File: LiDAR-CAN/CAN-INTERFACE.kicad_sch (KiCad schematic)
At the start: 0 parts

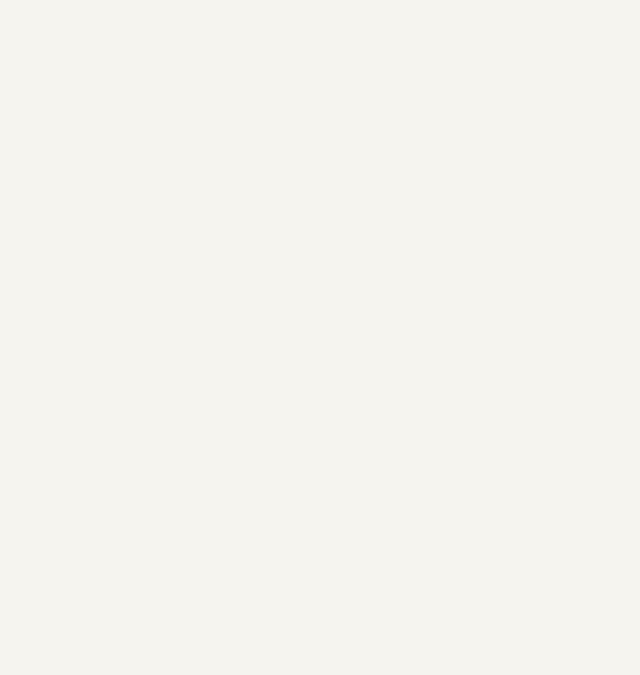
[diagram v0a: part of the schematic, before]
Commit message: Add main components in schematic sheets
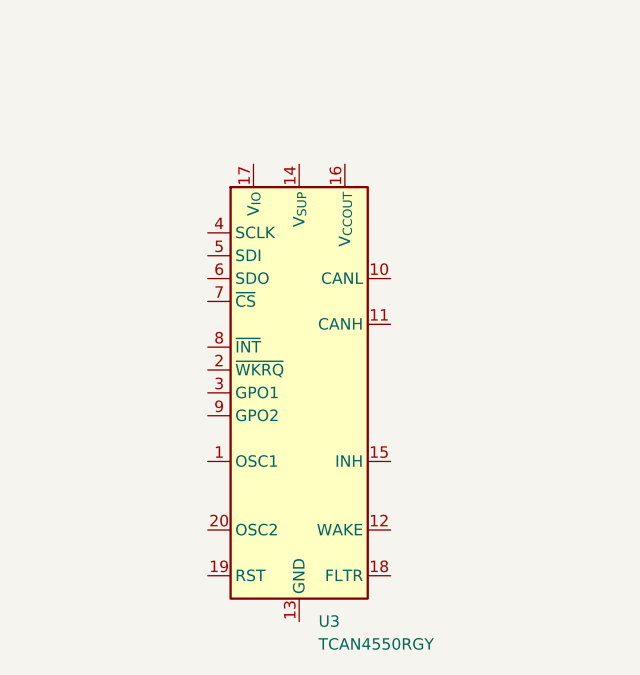
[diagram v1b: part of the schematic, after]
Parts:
- added U3: TCAN4550RGY, Package_DFN_QFN:Texas_RGY_R-PVQFN-N20_EP2.05x3.05mm, symbol Interface_CAN_LIN:TCAN4550RGY
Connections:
- new net: U3.13 (GND), U3.21 (GND)
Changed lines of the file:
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@@
+		)
+	)
+	(symbol
+		(lib_id "Interface_CAN_LIN:TCAN4550RGY")
+		(at 139.7 86.36 0)
+		(unit 1)
+		(exclude_from_sim no)
+		(in_bom yes)
+		(on_board yes)
+		(dnp no)
+		(fields_autoplaced yes)
+		(property "Reference" "U3"
+			(at 141.8433 111.76 0)
+			(effects
+				(font
+					(size 1.27 1.27)
+				)
+				(justify left)
+			)
+		)
+		(property "Value" "TCAN4550RGY"
+			(at 141.8433 114.3 0)
+			(effects
+				(font
+					(size 1.27 1.27)
+				)
+				(justify left)
+			)
+		)
+		(property "Footprint" "Package_DFN_QFN:Texas_RGY_R-PVQFN-N20_EP2.05x3.05mm"
+			(at 147.32 116.84 0)
+			(effects
+				(font
+					(size 1.27 1.27)
+					(italic yes)
+				)
+				(justify left)
+				(hide yes)
+			)
+		)
+		(property "Datasheet" "https://www.ti.com/lit/ds/symlink/tcan4550.pdf"
+			(at 147.32 114.3 0)
+			(effects
+				(font
+					(size 1.27 1.27)
+				)
+				(justify left)
+				(hide yes)
+			)
+		)
+		(property "Description" "CAN-FD controller with integrated transceiver, 5Mbps, 3.3V to 5V supply, SPI interface, VQFN-20"
+			(at 147.32 119.38 0)
+			(effects
+				(font
+					(size 1.27 1.27)
+				)
+				(justify left)
+				(hide yes)
+			)
+		)
+		(pin "5"
+		)
+		(pin "19"
+		)
+		(pin "16"
+		)
+		(pin "20"
+		)
+		(pin "4"
+		)
+		(pin "12"
+		)
+		(pin "8"
+		)
+		(pin "13"
+		)
+		(pin "6"
+		)
+		(pin "14"
+		)
+		(pin "3"
+		)
+		(pin "1"
+		)
+		(pin "2"
+		)
+		(pin "18"
+		)
+		(pin "9"
+		)
+		(pin "21"
+		)
+		(pin "10"
+		)
+		(pin "11"
+		)
+		(pin "15"
+		)
+		(pin "7"
+		)
+		(pin "17"
+		)
+		(instances
+			(project ""
+				(path "/56db6f21-0e4a-4321-bd8a-db37f1842dd9/acdb1e38-683e-41e3-b904-0eede9d7599d"
+					(reference "U3")
+					(unit 1)
+				)
+			)
 		)
 	)

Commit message: Add LiDAR Interface complete circuit
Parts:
- U3: Manufacturer (none) -> Texas Instruments
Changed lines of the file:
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@@
+			)
+		)
+		(property "Manufacturer" "Texas Instruments"
+			(at 139.7 86.36 0)
+			(effects
+				(font
+					(size 1.27 1.27)
+				)
+				(hide yes)
 			)
 		)

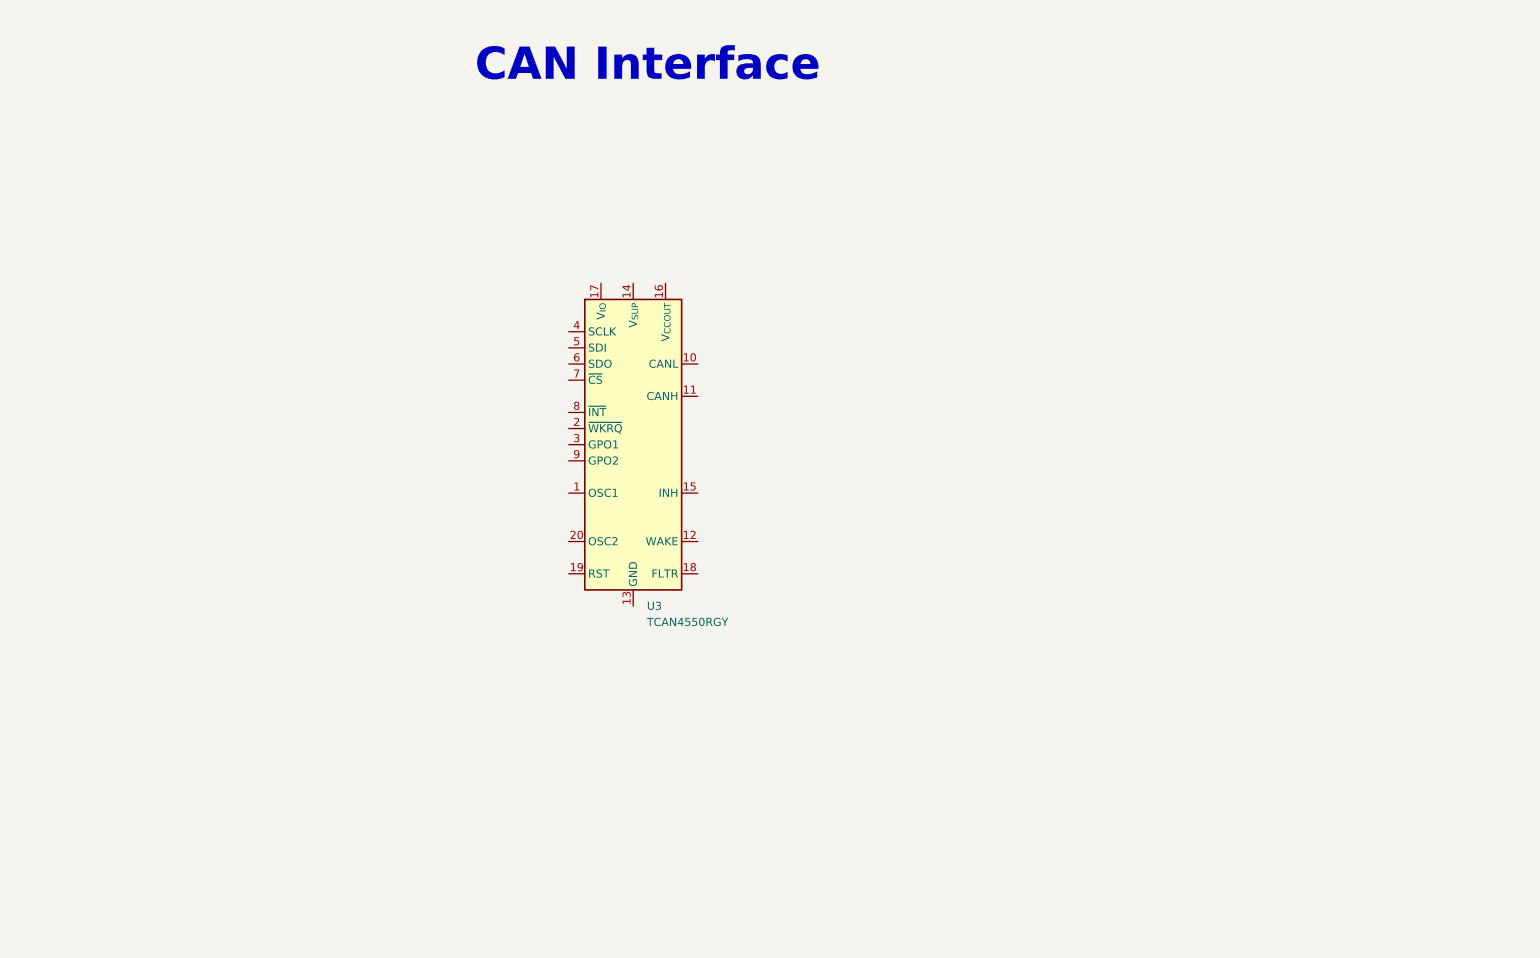
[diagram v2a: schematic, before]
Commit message: Add complete CAN Interface circuit
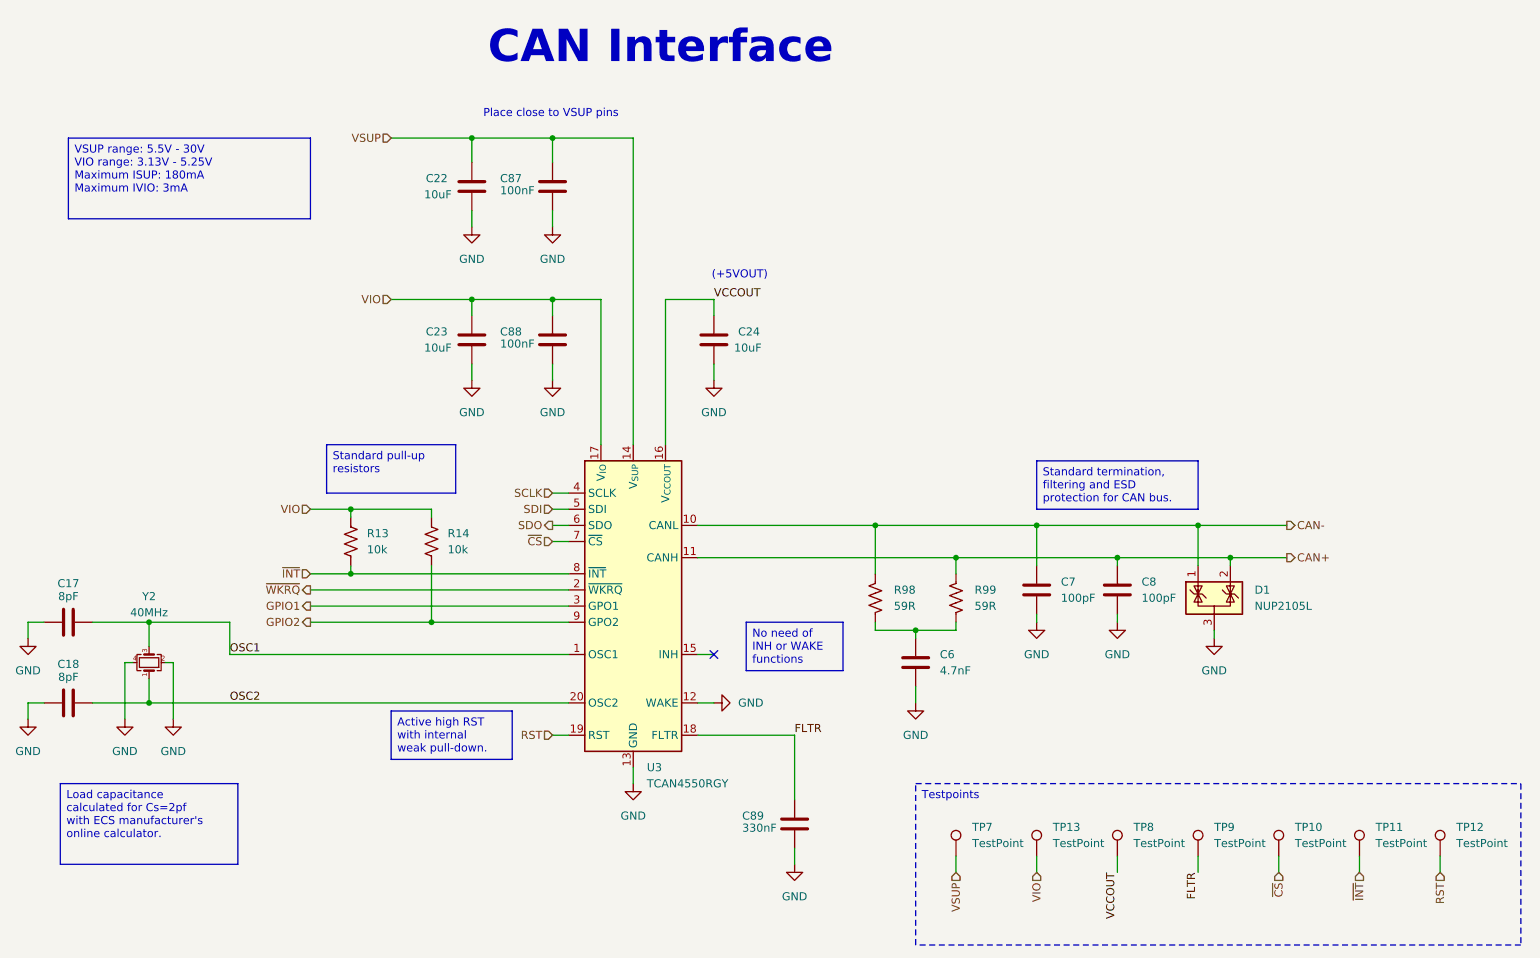
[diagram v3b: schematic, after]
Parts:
- added C17, C18: 8pF, Capacitor_SMD:C_0603_1608Metric, symbol Symbols:CAP CER 22PF 50V X7R 0603
- added C22, C23, C24: 10uF, Capacitor_SMD:C_0603_1608Metric, symbol Symbols:CAP CER 10UF 25V X5R 0603
- added C6: 4.7nF, Capacitor_SMD:C_0603_1608Metric, symbol Device:C
- added C7, C8: 100pF, Capacitor_SMD:C_0603_1608Metric, symbol Device:C
- added C87, C88: 100nF, Capacitor_SMD:C_0603_1608Metric, symbol Symbols:CAP CER 0.1UF 50V X7R 0603
- added C89: 330nF, Capacitor_SMD:C_0603_1608Metric, symbol Symbols:CAP CER 0.1UF 50V X7R 0603
- added D1: NUP2105L, Package_TO_SOT_SMD:SOT-23, symbol Power_Protection:NUP2105L
- added R13, R14: 10k, Resistor_SMD:R_0603_1608Metric, symbol Device:R_US
- added R98, R99: 59R, Resistor_SMD:R_0603_1608Metric, symbol Symbols:RES 1.2K OHM 5% 1/10W 0603
- added TP10, TP11, TP12, TP13, TP7, TP8, TP9: TestPoint, TestPoint:TestPoint_Pad_D1.5mm, symbol Connector:TestPoint
- added Y2: 40MHz, Crystal:Crystal_SMD_2016-4Pin_2.0x1.6mm, symbol Device:Crystal_GND24_Small
- U3: MPN (none) -> TCAN4550RGYRQ1
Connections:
- net OSC1: now reaches U3.1 (OSC1)
- net OSC1: now also C17.2, Y2.3
- net CAN-: now reaches U3.10 (CANL)
- net CAN-: now also C7.1, D1.1 (K), R98.2
- net CAN+: now reaches U3.11 (CANH)
- net CAN+: now also C8.1, D1.2 (K), R99.2
- net GND: now reaches U3.12 (WAKE)
- net GND: now also U3.13 (GND), U3.21 (GND), C17.1, C18.1, C22.2, C23.2, C24.2, C6.2, C7.2, C8.2, C87.1, C88.1, C89.1, D1.3 (A), Y2.2, Y2.4
- net VSUP: now reaches U3.14 (V_{SUP})
- net VSUP: now also C22.1, C87.2, TP7.1
- net VCCOUT: now reaches U3.16 (V_{CCOUT})
- net VCCOUT: now also C24.1, TP8.1
- net VIO: now reaches U3.17 (V_{IO})
- net VIO: now also C23.1, C88.2, R13.1, R14.1, TP13.1
- net FLTR: now reaches U3.18 (FLTR)
- net FLTR: now also C89.2, TP9.1
- net RST: now reaches U3.19 (RST)
- net RST: now also TP12.1
- net ~{WKRQ}: now reaches U3.2 (~{WKRQ})
- net OSC2: now reaches U3.20 (OSC2)
- net OSC2: now also C18.2, Y2.1
- net GPIO1: now reaches U3.3 (GPO1)
- net SCLK: now reaches U3.4 (SCLK)
- net SDI: now reaches U3.5 (SDI)
- net SDO: now reaches U3.6 (SDO)
- net ~{CS}: now reaches U3.7 (~{CS})
- net ~{CS}: now also TP10.1
- net ~{INT}: now reaches U3.8 (~{INT})
- net ~{INT}: now also R13.2, TP11.1
- net GPIO2: now reaches U3.9 (GPO2)
- net GPIO2: now also R14.2
- new net: C6.1, R98.1, R99.1
- no-connect marks 0 -> 1
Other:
- note added: "(+5VOUT)"
- note added: "Place close to VSUP pins"
- moved on the sheet: U3

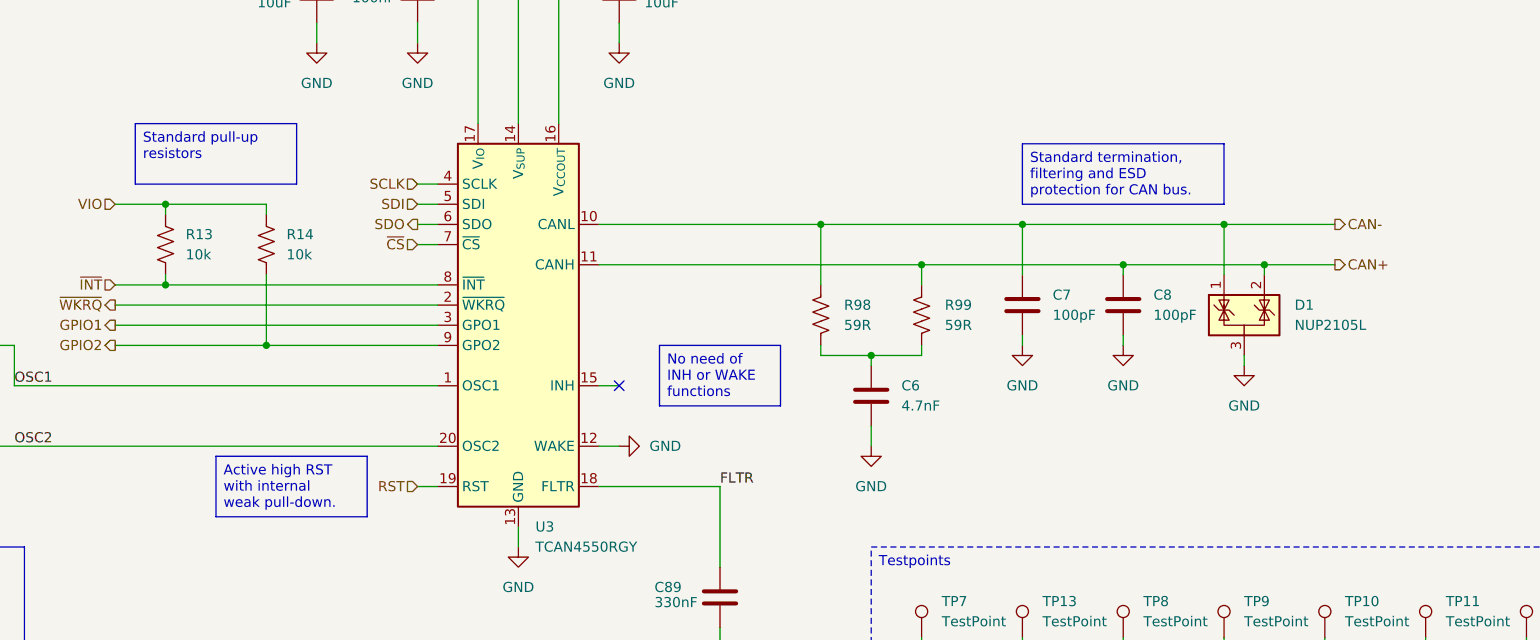
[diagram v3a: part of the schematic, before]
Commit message: Add external connector circuit
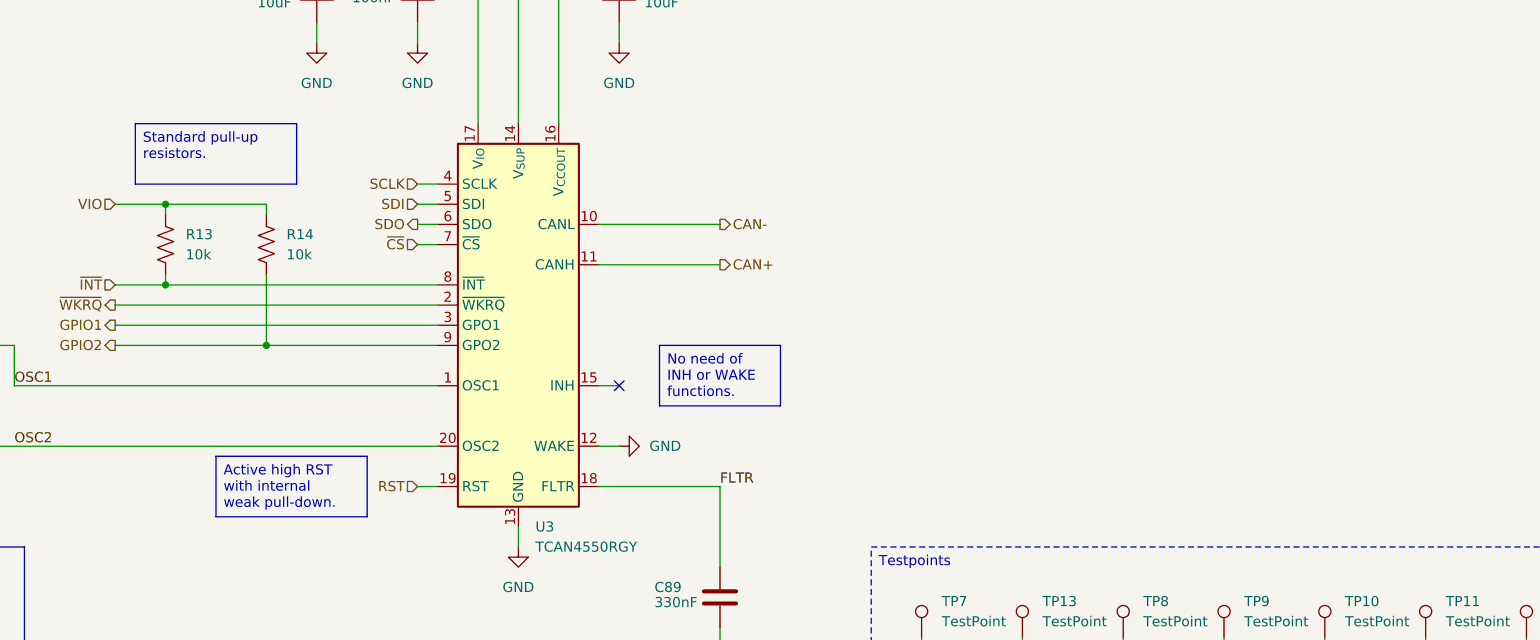
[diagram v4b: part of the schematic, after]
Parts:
- removed C6: 4.7nF, Capacitor_SMD:C_0603_1608Metric, symbol Device:C
- removed C7, C8: 100pF, Capacitor_SMD:C_0603_1608Metric, symbol Device:C
- removed D1: NUP2105L, Package_TO_SOT_SMD:SOT-23, symbol Power_Protection:NUP2105L
- removed R98, R99: 59R, Resistor_SMD:R_0603_1608Metric, symbol Symbols:RES 1.2K OHM 5% 1/10W 0603
